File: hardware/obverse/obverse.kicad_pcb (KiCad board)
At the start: 2 copper layers, 40 x 40 mm, 13 parts, among them T42 TestPoint_THTPad_D1.0mm_Drill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, T43 TestPoint_THTPad_D1.0mm_Drill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, T44 TestPoint_THTPad_D1.0mm_Drill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, T45 TestPoint_THTPad_D1.0mm_Drill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, T46 TestPoint_THTPad_D1.0mm_Drill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, T48 TestPoint_THTPad_D1.0mm_Drill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, T49 TestPoint_THTPad_D1.0mm_Drill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, T50 TestPoint_THTPad_D1.0mm_Drill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, T51 TestPoint_THTPad_D1.0mm_Drill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, T52 TestPoint_THTPad_D1.0mm_Drill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

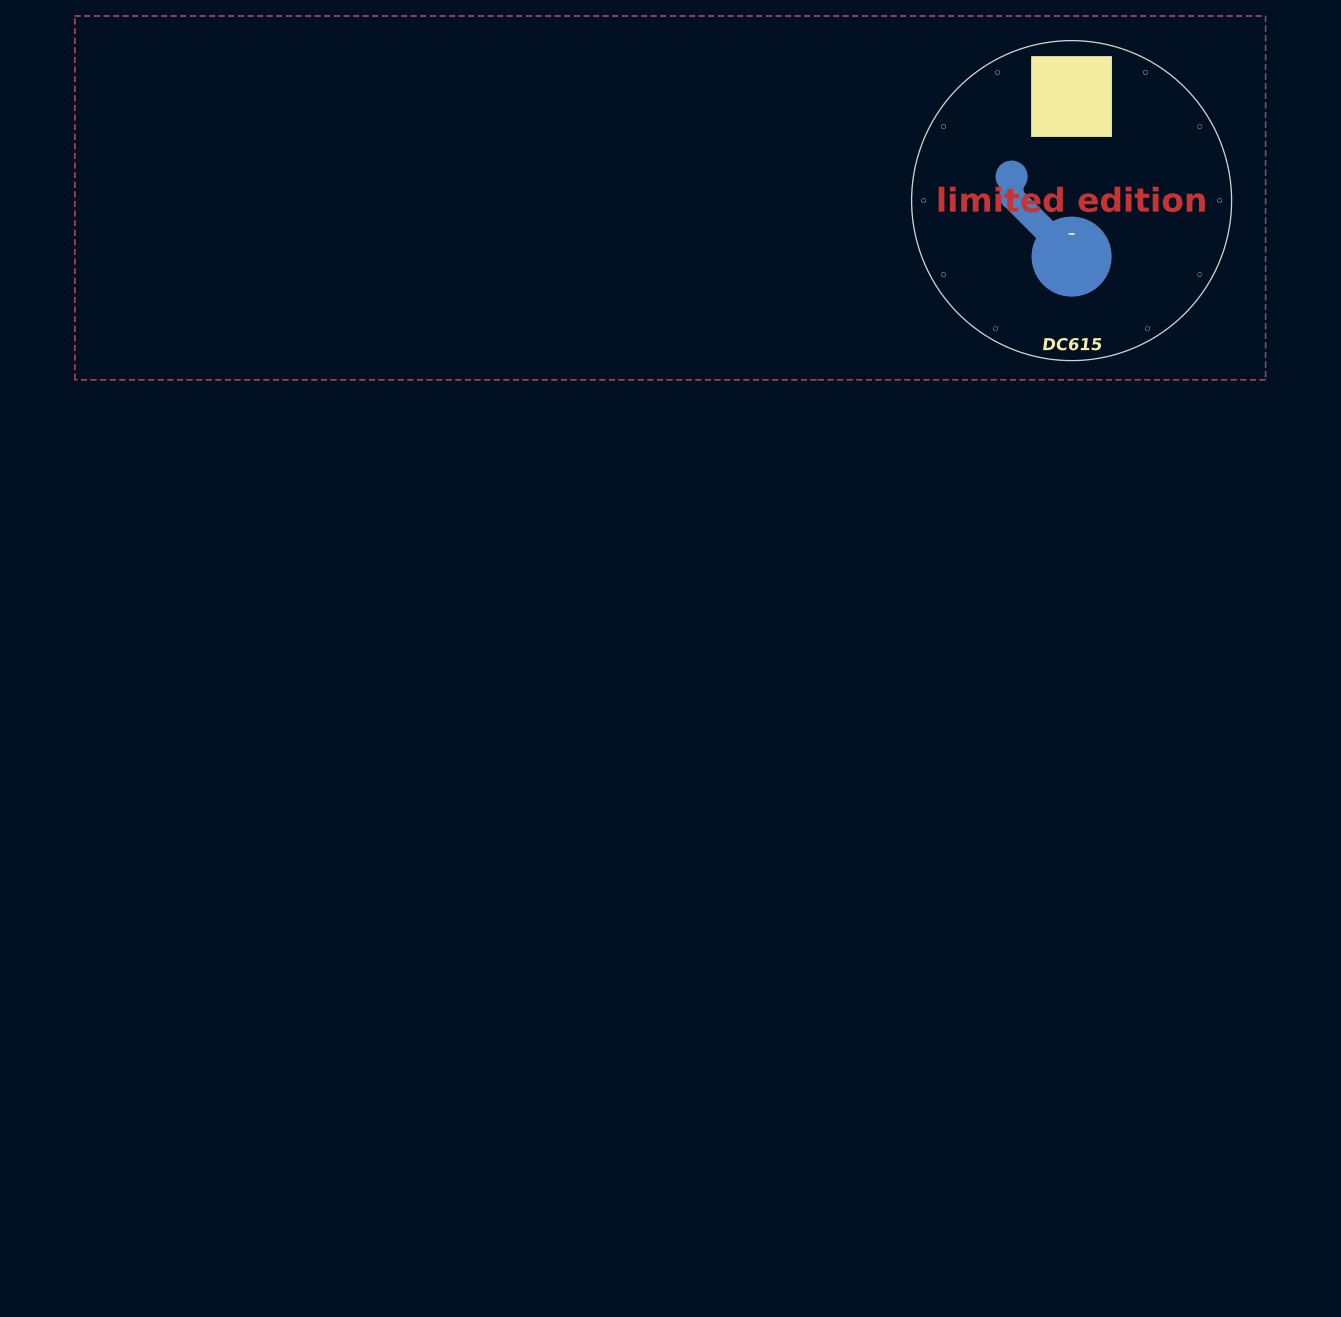
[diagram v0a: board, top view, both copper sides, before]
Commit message: separate boards and generate fab files
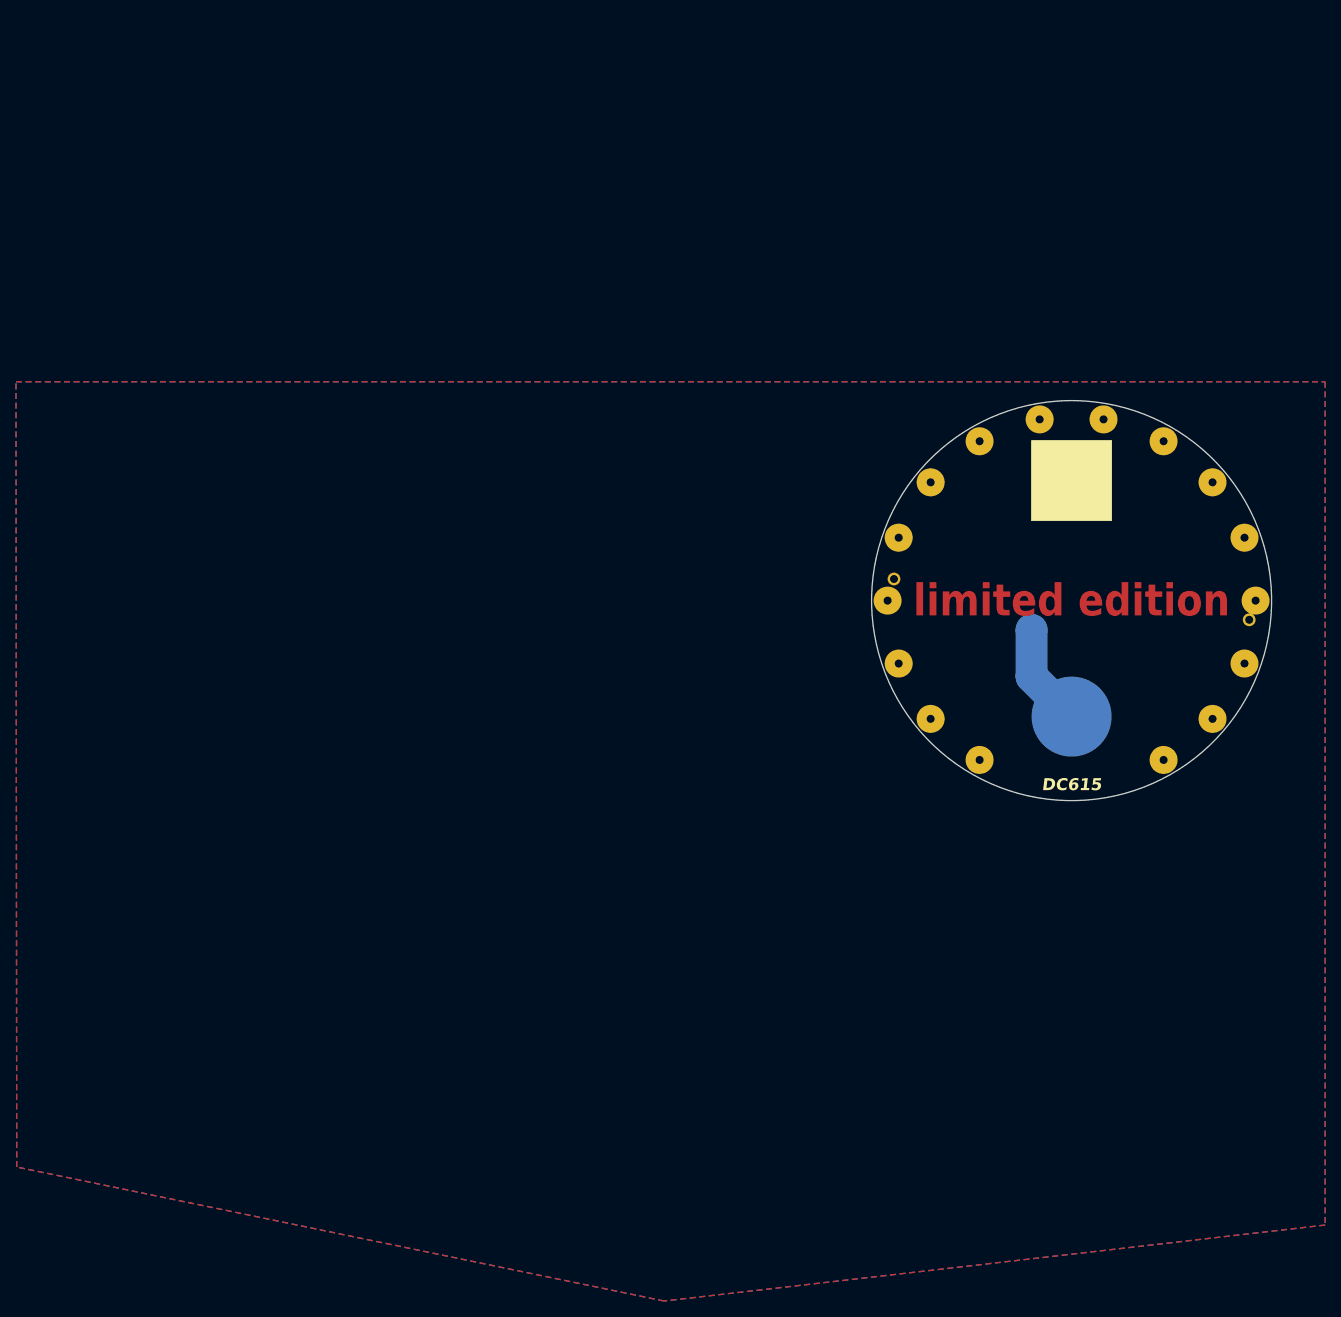
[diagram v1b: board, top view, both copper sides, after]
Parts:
- removed T42, T43, T44, T45, T46, T48, T49, T50, T51, T52: TestPoint_THTPad_D1.0mm_Drill0.5mm, TestPoint:TestPoint_THTPad_D1.0mm_Drill0.5mm
- added align-o1: , , F.Cu at (127.8, 97.3)
- added align-o2: , , F.Cu at (172.2, 102.4)
- added aperture-D1: TestPoint_THTPad_D1.0mm_Drill0.5mm, TestPoint:TestPoint_THTPad_D1.0mm_Drill0.5mm, F.Cu at (138.5, 119.9)
- added aperture-D10: TestPoint_THTPad_D1.0mm_Drill0.5mm, TestPoint:TestPoint_THTPad_D1.0mm_Drill0.5mm, F.Cu at (161.5, 80.1)
- added aperture-D11: TestPoint_THTPad_D1.0mm_Drill0.5mm, TestPoint:TestPoint_THTPad_D1.0mm_Drill0.5mm, F.Cu at (167.6, 85.2)
- added aperture-D12: TestPoint_THTPad_D1.0mm_Drill0.5mm, TestPoint:TestPoint_THTPad_D1.0mm_Drill0.5mm, F.Cu at (171.6, 92.1)
- added aperture-D13: TestPoint_THTPad_D1.0mm_Drill0.5mm, TestPoint:TestPoint_THTPad_D1.0mm_Drill0.5mm, F.Cu at (173.0, 100.0)
- added aperture-D14: TestPoint_THTPad_D1.0mm_Drill0.5mm, TestPoint:TestPoint_THTPad_D1.0mm_Drill0.5mm, F.Cu at (171.6, 107.9)
- added aperture-D15: TestPoint_THTPad_D1.0mm_Drill0.5mm, TestPoint:TestPoint_THTPad_D1.0mm_Drill0.5mm, F.Cu at (167.6, 114.8)
- added aperture-D16: TestPoint_THTPad_D1.0mm_Drill0.5mm, TestPoint:TestPoint_THTPad_D1.0mm_Drill0.5mm, F.Cu at (161.5, 119.9)
- added aperture-D2: TestPoint_THTPad_D1.0mm_Drill0.5mm, TestPoint:TestPoint_THTPad_D1.0mm_Drill0.5mm, F.Cu at (132.4, 114.8)
- added aperture-D3: TestPoint_THTPad_D1.0mm_Drill0.5mm, TestPoint:TestPoint_THTPad_D1.0mm_Drill0.5mm, F.Cu at (128.4, 107.9)
- added aperture-D4: TestPoint_THTPad_D1.0mm_Drill0.5mm, TestPoint:TestPoint_THTPad_D1.0mm_Drill0.5mm, F.Cu at (127.0, 100.0)
- added aperture-D5: TestPoint_THTPad_D1.0mm_Drill0.5mm, TestPoint:TestPoint_THTPad_D1.0mm_Drill0.5mm, F.Cu at (128.4, 92.1)
- added aperture-D6: TestPoint_THTPad_D1.0mm_Drill0.5mm, TestPoint:TestPoint_THTPad_D1.0mm_Drill0.5mm, F.Cu at (132.4, 85.2)
- added aperture-D7: TestPoint_THTPad_D1.0mm_Drill0.5mm, TestPoint:TestPoint_THTPad_D1.0mm_Drill0.5mm, F.Cu at (138.5, 80.1)
- added aperture-D8: TestPoint_THTPad_D1.0mm_Drill0.5mm, TestPoint:TestPoint_THTPad_D1.0mm_Drill0.5mm, F.Cu at (146.0, 77.3)
- added aperture-D9: TestPoint_THTPad_D1.0mm_Drill0.5mm, TestPoint:TestPoint_THTPad_D1.0mm_Drill0.5mm, F.Cu at (154.0, 77.3)
- moved + 57.5 mm to (150.0, 114.5)
- moved B2 57.5 mm to (150.0, 114.5)
- moved contact-o1 56.7 mm to (145.0, 103.7)
- renumbered REF** to contact-o1
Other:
- board size 40 x 40 mm -> 50 x 50 mm
- board text added: "import QR SVG scale 0.2"
- board text removed: "-"

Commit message: separate into fab-able parts
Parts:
- moved align-o2 50.0 mm to (172.2, 52.4)
- moved aperture-D11 50.0 mm to (167.6, 35.2)
- moved aperture-D6 50.0 mm to (132.4, 35.2)
- moved + 50.0 mm to (150.0, 64.5)
- moved B2 50.0 mm to (150.0, 64.5)
- moved align-o1 50.0 mm to (127.8, 47.3)
- moved aperture-D1 50.0 mm to (138.5, 69.9)
- moved aperture-D10 50.0 mm to (161.5, 30.1)
- moved aperture-D12 50.0 mm to (171.6, 42.1)
- moved aperture-D13 50.0 mm to (173.0, 50.0)
- moved aperture-D14 50.0 mm to (171.6, 57.9)
- moved aperture-D15 50.0 mm to (167.6, 64.8)
- moved aperture-D16 50.0 mm to (161.5, 69.9)
- moved aperture-D2 50.0 mm to (132.4, 64.8)
- moved aperture-D3 50.0 mm to (128.4, 57.9)
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
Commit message: cleanup fab files
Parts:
- added align-o2: , , F.Cu at (172.2, 47.3)
- added align-o3: , , F.Cu at (127.8, 52.4)
- renumbered align-o2 to align-o4
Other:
- board text removed: "import QR SVG scale 0.2"

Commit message: separate boards
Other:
- board text added: "1. apply solder paste, stack internal board, reflow"
- board text added: "2. apply solder paste, reflow to thicken pad"
- board text added: "E PLVRIBVS VNVM"
- board text added: "to align use 1.0mm dia pins"
- board text removed: "DC615"
- board text removed: "limited edition"
